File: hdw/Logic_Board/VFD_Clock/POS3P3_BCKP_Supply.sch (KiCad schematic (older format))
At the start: 0 parts

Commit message: Changed to configurable discrete gates, added VBAT stuff
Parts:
- added BT?: TL-4903/P, symbol Device:Battery_Cell
- added BT?: CR2032, Battery_Holders:Keystone_1058_1x2032-CoinCell, symbol Device:Battery_Cell
- added BT?: BR-2/3AE5SPN, Custom Footprints Library:BR-2_3AE5SPN, symbol Device:Battery_Cell
- added C? (x6): 10uF, Capacitors_SMD:C_1206, symbol Custom_Library:C_Custom
- added C?: 0.1uF, Capacitors_SMD:C_0603, symbol Custom_Library:C_Custom
- added L?: 2.2uH, symbol Custom_Library:L_Custom
- added R? (x2): 562k, Resistors_SMD:R_0603, symbol Custom_Library:R_Custom
- added R?: 1.07M, Resistors_SMD:R_0603, symbol Custom_Library:R_Custom
- added R?: 196k, Resistors_SMD:R_0603, symbol Custom_Library:R_Custom
- added R?: 84.5k, Resistors_SMD:R_0603, symbol Custom_Library:R_Custom
- added R?: 45.3k, Resistors_SMD:R_0603, symbol Custom_Library:R_Custom
- added R?: 100, Resistors_SMD:R_0603, symbol Custom_Library:R_Custom
- added R?: 10k, Resistors_SMD:R_0603, symbol Custom_Library:R_Custom
- added R? (x2): 0, symbol Custom_Library:R_Custom
- added U?: LTC4419DD, Housings_DFN_QFN:DFN-10-1EP_3x3mm_Pitch0.5mm, symbol Custom_Library:LTC4419DD
- added U?: TPS22929D, Package_TO_SOT_SMD:SOT-23-6, symbol Power_Management:TPS22929D
- added U?: TPS63001, Package_SON:Texas_DRC0010J_ThermalVias, symbol Regulator_Switching:TPS63001
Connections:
- new net: R?.1, R?.2, U?.3 (ADJ)
- new net: C?.1, C?.1, R?.1, R?.2, R?.2, U?.5 (VIN), U?.8 (OUT)
- new net: R?.1, R?.2, U?.9 (CMP2)
- new net: BT?.1 (+), BT?.1 (+), BT?.1 (+), U?.4 (VIN), U?.6 (VIN)
- new net: L?.2, U?.2 (L2)
- new net: L?.1, U?.4 (L1)
- new net: C?.1, R?.1, U?.6 (EN), U?.7 (PS/SYNC), U?.8 (VINA)
- new net +3.3V_BCKP: C?.1, C?.1, R?.1, R?.2, U?.1 (VOUT), U?.10 (FB)
- new net +3V3: C?.1, R?.1, R?.1, R?.2, U?.1 (V1)
- new net BCKUP_ON: R?.2, U?.7 (V2ON)
- new net GND: BT?.2 (-), BT?.2 (-), BT?.2 (-), C?.2, C?.2, C?.2, C?.2, C?.2, C?.2, C?.2, R?.2, R?.2, R?.2, U?.11 (GND), U?.11 (PGND), U?.2 (CMP1), U?.2 (GND), U?.3 (PGND), U?.4 (GND), U?.5 (GND), U?.9 (GND)
- new net VBAT: C?.1, R?.1, U?.1 (VOUT), U?.10 (V2)
- new net VBAT_EN: R?.1, U?.3 (ON)
- new net VBAT_PGOOD: R?.1, U?.6 (CMPOUT2)
- no-connect marks 0 -> 1
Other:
- note added: "V1 to V2 switchover\n@ POS3P3 = +3.0V"
- note added: "VBAT undervoltage\n@ 2.5V"

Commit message: Few hdw tweaks
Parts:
- removed R?: 0, symbol Custom_Library:R_Custom
- added R?: 0, symbol Custom_Library:R_Custom
- BT?: CFG DNP -> (none); Digi-Key PN (none) -> DNP
- BT?: CFG DNP -> (none); Digi-Key PN P226-ND -> DNP
- R?: CFG DNP -> (none); Digi-Key PN RMCF0805ZT0R00CT-ND -> DNP
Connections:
- net +3.3V_BCKP: now also R?.2
- net at C?.1, C?.1, R?.2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: now also R?.1
- net BCKUP_ON renamed BCKP_ON
- net VBAT_EN renamed VBAT_Enable
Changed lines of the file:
@@
 	3820 6350 3820 6430
 Text GLabel 3740 6350 0    50   Input ~ 0
-VBAT_EN
+VBAT_Enable
 Wire Wire Line
 	3740 6350 3820 6350
@@
 F 2 "Battery_Holders:Keystone_1058_1x2032-CoinCell" V 2130 6390 50  0001 C CNN
 F 3 "~" V 2130 6390 50  0001 C CNN
-F 4 "DNP" H 2310 6250 50  0000 C CNN "CFG"
+F 4 "DNP" H 2310 6240 50  0000 C CNN "Digi-Key PN"
 	1    2130 6330
 	1    0    0    -1
@@
 VBAT undervoltage\n@ 2.5V
 Text GLabel 5600 4670 2    50   Output ~ 0
-BCKUP_ON
+BCKP_ON
 Wire Wire Line
 	5600 4670 5120 4670
@@
 	-1   0    0    1
 $EndComp
-$Comp
-L Custom_Library:R_Custom R?
-U 1 1 5E30F0F6
-P 7180 1330
-F 0 "R?" V 7080 1330 50  0000 C CNN
-F 1 "0" V 7180 1330 50  0000 C CNN
-F 2 "" H 7180 1330 50  0001 C CNN
-F 3 "" H 7180 1330 50  0001 C CNN
-F 4 "0805" V 7280 1330 50  0000 C CNN "display_footprint"
-F 5 "1%" V 7380 1330 50  0000 C CNN "Tolerance"
-F 6 "1/10W" V 7480 1330 50  0000 C CNN "Wattage"
-F 7 "RMCF0805ZT0R00CT-ND" H 7480 1730 60  0001 C CNN "Digi-Key PN"
-F 8 "DNP" V 7010 1330 50  0000 C CNN "CFG"
-	1    7180 1330
-	0    -1   -1   0
-$EndComp
 Wire Wire Line
 	7030 1330 5560 1330
@@
 F 5 "1%" V 3650 1330 50  0000 C CNN "Tolerance"
 F 6 "1/10W" V 3750 1330 50  0000 C CNN "Wattage"
-F 7 "RMCF0805ZT0R00CT-ND" H 3750 1730 60  0001 C CNN "Digi-Key PN"
-F 8 "DNP" V 3280 1330 50  0000 C CNN "CFG"
+F 7 "DNP" V 3260 1330 60  0000 C CNN "Digi-Key PN"
 	1    3450 1330
 	0    -1   -1   0
@@
 F 2 "Custom Footprints Library:BR-2_3AE5SPN" V 1220 6390 50  0001 C CNN
 F 3 "~" V 1220 6390 50  0001 C CNN
-F 4 "DNP" H 1400 6250 50  0000 C CNN "CFG"
-F 5 "P226-ND" H 1220 6330 50  0001 C CNN "Digi-Key PN"
+F 4 "DNP" H 1400 6250 50  0000 C CNN "Digi-Key PN"
 	1    1220 6330
 	1    0    0    -1
@@
 	1220 6050 1220 6130
 Connection ~ 2130 6050
+$Comp
+L Custom_Library:R_Custom R?
+U 1 1 5E3DFB0F
+P 7180 1330
+F 0 "R?" V 7080 1330 50  0000 C CNN
+F 1 "0" V 7180 1330 50  0000 C CNN
+F 2 "" H 7180 1330 50  0001 C CNN
+F 3 "" H 7180 1330 50  0001 C CNN
+F 4 "0805" V 7280 1330 50  0000 C CNN "display_footprint"
+F 5 "1%" V 7380 1330 50  0000 C CNN "Tolerance"
+F 6 "1/10W" V 7480 1330 50  0000 C CNN "Wattage"
+F 7 "DNP" V 6990 1330 60  0000 C CNN "Digi-Key PN"
+	1    7180 1330
+	0    -1   -1   0
+$EndComp
 $EndSCHEMATC

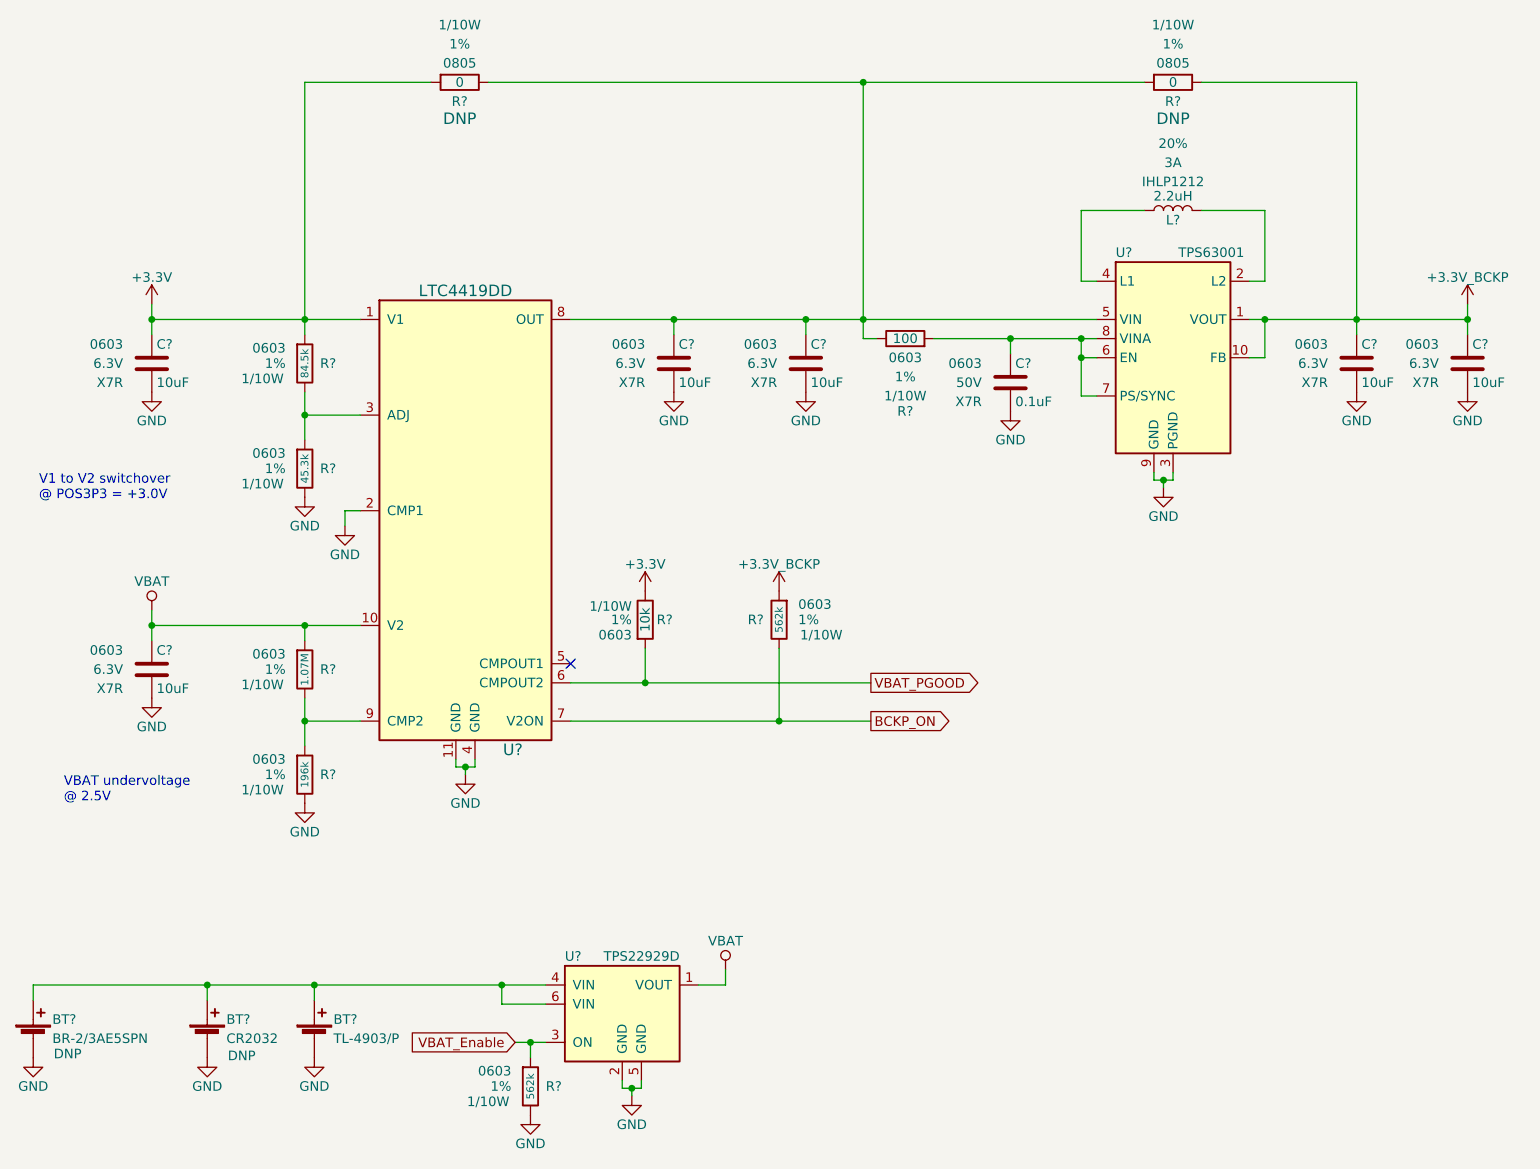
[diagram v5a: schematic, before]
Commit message: Few fixes, added BLE
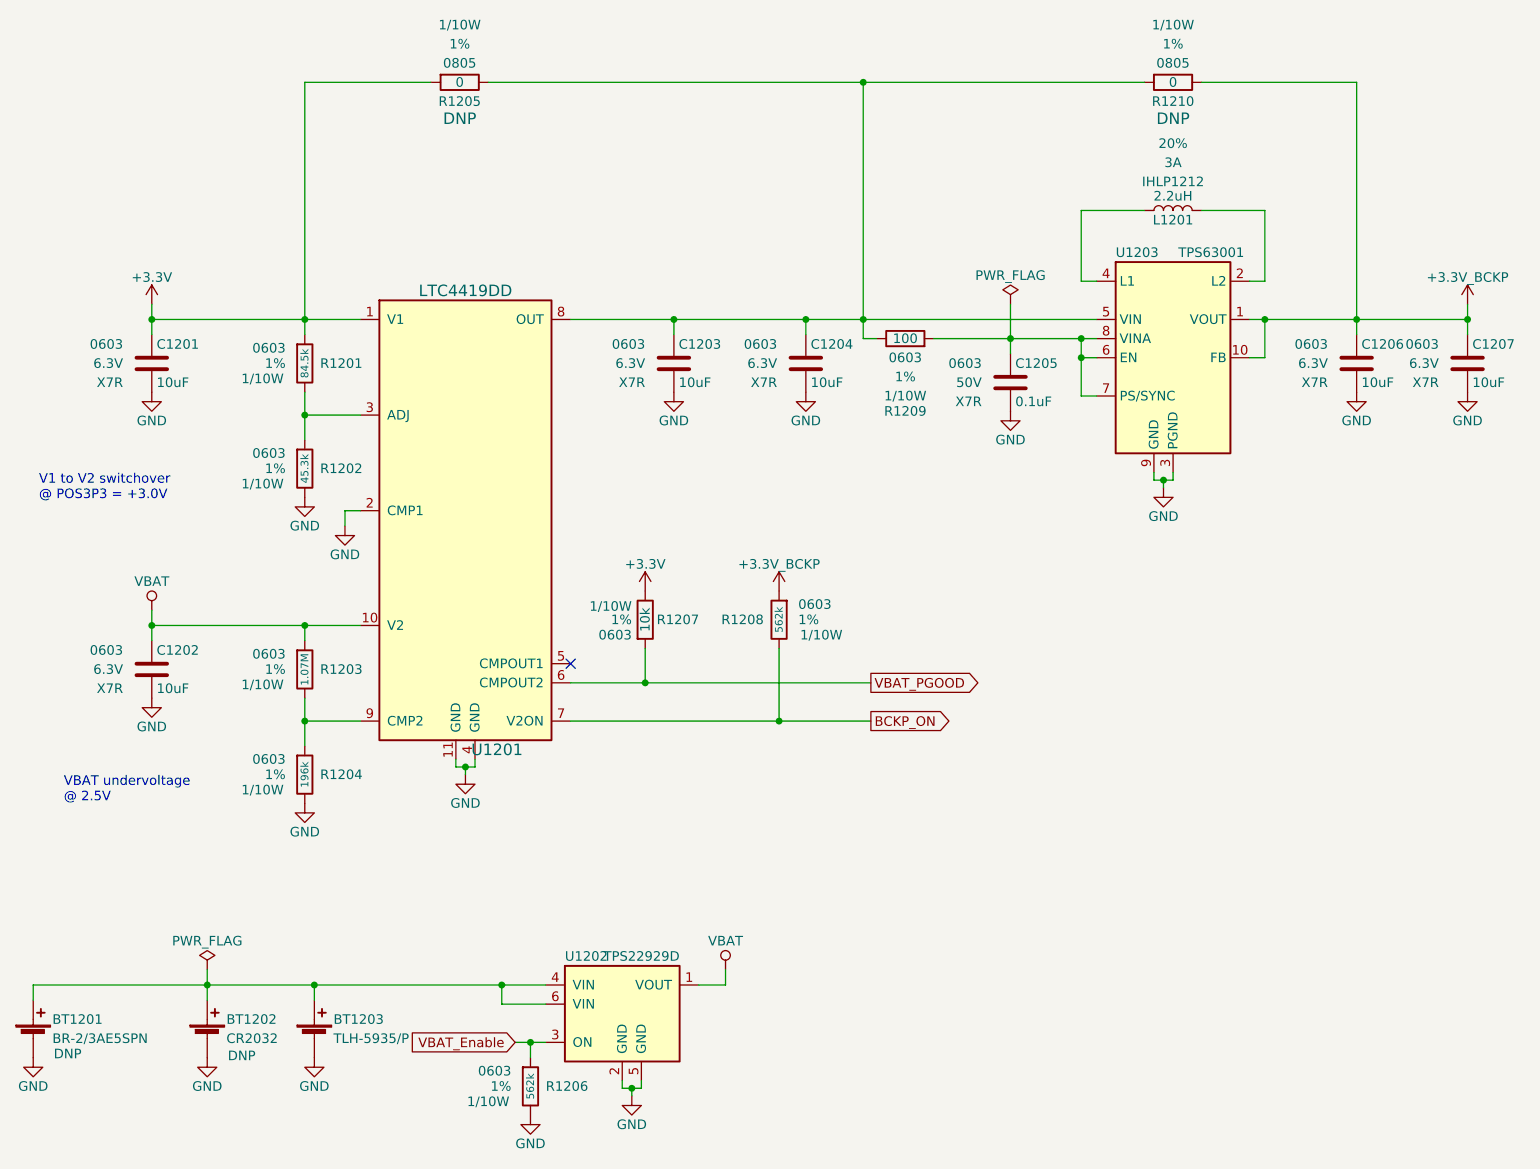
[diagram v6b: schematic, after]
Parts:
- BT1203: renamed from BT?; value TL-4903/P -> TLH-5935/P; footprint (none) -> Custom Footprints Library:TLH-5935; Digi-Key PN 439-1070-ND -> 439-1038-ND
- C1201, C1202, C1203, C1204, C1206, C1207: renamed from C?; Digi-Key PN (none) -> 399-4938-1-ND
- L1201: renamed from L?; footprint (none) -> Inductors_SMD:L_Vishay_IHLP-1212
- R1201: renamed from R?; Digi-Key PN (none) -> RMCF0603FT84K5CT-ND
- R1202: renamed from R?; Digi-Key PN (none) -> RMCF0603FT45K3CT-ND
- R1203: renamed from R?; Digi-Key PN (none) -> 541-1.07MHCT-ND
- R1204: renamed from R?; Digi-Key PN (none) -> RMCF0603FT196KCT-ND
- R1205, R1210: renamed from R?; footprint (none) -> Resistors_SMD:R_0805
- U1202: renamed from U?; Digi-Key PN (none) -> 296-38579-1-ND
- gave numbers to parts that had none: 9

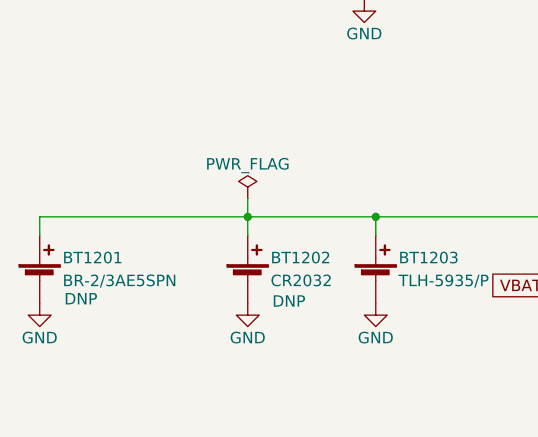
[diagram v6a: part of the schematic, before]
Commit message: Finished arranging groups of parts
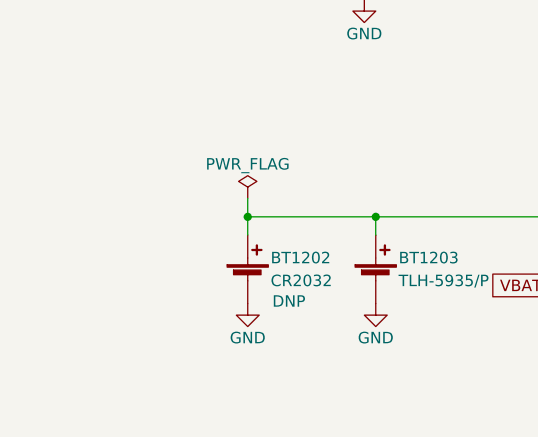
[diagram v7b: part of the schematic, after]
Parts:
- removed BT1201: BR-2/3AE5SPN, Custom Footprints Library:BR-2_3AE5SPN, symbol Device:Battery_Cell
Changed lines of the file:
@@
 Wire Wire Line
 	2640 1330 2640 2570
-$Comp
-L Device:Battery_Cell BT1201
-U 1 1 5E31F428
-P 1220 6330
-F 0 "BT1201" H 1320 6430 50  0000 L CNN
-F 1 "BR-2/3AE5SPN" H 1320 6330 50  0000 L CNN
-F 2 "Custom Footprints Library:BR-2_3AE5SPN" V 1220 6390 50  0001 C CNN
-F 3 "~" V 1220 6390 50  0001 C CNN
-F 4 "DNP" H 1400 6250 50  0000 C CNN "Digi-Key PN"
-	1    1220 6330
-	1    0    0    -1
-$EndComp
-$Comp
-L power:GND #PWR?
-U 1 1 5E3203B8
-P 1220 6430
-AR Path="/5CB7718D/5E3203B8" Ref="#PWR?"  Part="1"
-AR Path="/5E0DC082/5E3203B8" Ref="#PWR?"  Part="1"
-AR Path="/5E0F9110/5E3203B8" Ref="#PWR?"  Part="1"
-AR Path="/5A557C58/5E3203B8" Ref="#PWR01201"  Part="1"
-F 0 "#PWR01201" H 1220 6180 50  0001 C CNN
-F 1 "GND" H 1220 6280 50  0000 C CNN
-F 2 "" H 1220 6430 50  0001 C CNN
-F 3 "" H 1220 6430 50  0001 C CNN
-	1    1220 6430
-	1    0    0    -1
-$EndComp
-Wire Wire Line
-	2130 6050 1220 6050
-Wire Wire Line
-	1220 6050 1220 6130
 Connection ~ 2130 6050
 $Comp

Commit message: Started routing
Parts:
- added TP1201, TP1202: TP, Custom Footprints Library:Test_Point, symbol Custom_Library:TP
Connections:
- net +3.3V_BCKP: now also TP1202.1 (TP)
- net VBAT: now also TP1201.1 (TP)
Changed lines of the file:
@@
 Wire Wire Line
 	6330 2490 6330 2670
+$Comp
+L Custom_Library:TP TP?
+U 1 1 5E426A4D
+P 8140 1250
+AR Path="/5C1D5CD8/5E426A4D" Ref="TP?"  Part="1"
+AR Path="/5C1D5C9E/5E426A4D" Ref="TP?"  Part="1"
+AR Path="/5C1E3A08/5E426A4D" Ref="TP?"  Part="1"
+AR Path="/5D779AE1/5E426A4D" Ref="TP?"  Part="1"
+AR Path="/5CB7718D/5E426A4D" Ref="TP?"  Part="1"
+AR Path="/5E0DC082/5E426A4D" Ref="TP?"  Part="1"
+AR Path="/5E0F9110/5E426A4D" Ref="TP?"  Part="1"
+AR Path="/5A557C58/5E426A4D" Ref="TP1202"  Part="1"
+F 0 "TP1202" H 8140 1400 50  0000 C CNN
+F 1 "TP" H 8140 1400 50  0001 C CNN
+F 2 "Custom Footprints Library:Test_Point" H 8140 1250 60  0001 C CNN
+F 3 "" H 8140 1250 60  0000 C CNN
+	1    8140 1250
+	1    0    0    -1
+$EndComp
+Wire Wire Line
+	8140 1250 8140 1330
+Connection ~ 8140 1330
+$Comp
+L Custom_Library:TP TP?
+U 1 1 5E42B4A2
+P 5220 5970
+AR Path="/5C1D5CD8/5E42B4A2" Ref="TP?"  Part="1"
+AR Path="/5C1D5C9E/5E42B4A2" Ref="TP?"  Part="1"
+AR Path="/5C1E3A08/5E42B4A2" Ref="TP?"  Part="1"
+AR Path="/5D779AE1/5E42B4A2" Ref="TP?"  Part="1"
+AR Path="/5CB7718D/5E42B4A2" Ref="TP?"  Part="1"
+AR Path="/5E0DC082/5E42B4A2" Ref="TP?"  Part="1"
+AR Path="/5E0F9110/5E42B4A2" Ref="TP?"  Part="1"
+AR Path="/5A557C58/5E42B4A2" Ref="TP1201"  Part="1"
+F 0 "TP1201" H 5220 6120 50  0000 C CNN
+F 1 "TP" H 5220 6120 50  0001 C CNN
+F 2 "Custom Footprints Library:Test_Point" H 5220 5970 60  0001 C CNN
+F 3 "" H 5220 5970 60  0000 C CNN
+	1    5220 5970
+	1    0    0    -1
+$EndComp
+Wire Wire Line
+	5220 5970 5220 6050
+Wire Wire Line
+	5220 6050 4840 6050
+Connection ~ 4840 6050
 $EndSCHEMATC
